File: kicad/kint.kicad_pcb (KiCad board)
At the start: 2 copper layers, 107.9 x 86 mm, 24 parts, among them J1 THUMB_RIGHT_SPC_KB600, J2 LEFT_13_LT, J3 TOP_LEFT, J4 TOP_RIGHT, J5 THUMB_LEFT_BAK, J6 THUMB_RIGHT_SPC, J7 RIGHT_13_DOWN, J8 THUMB_LEFT_BAK_KB600, U1 TEENSY_3.5/3.6

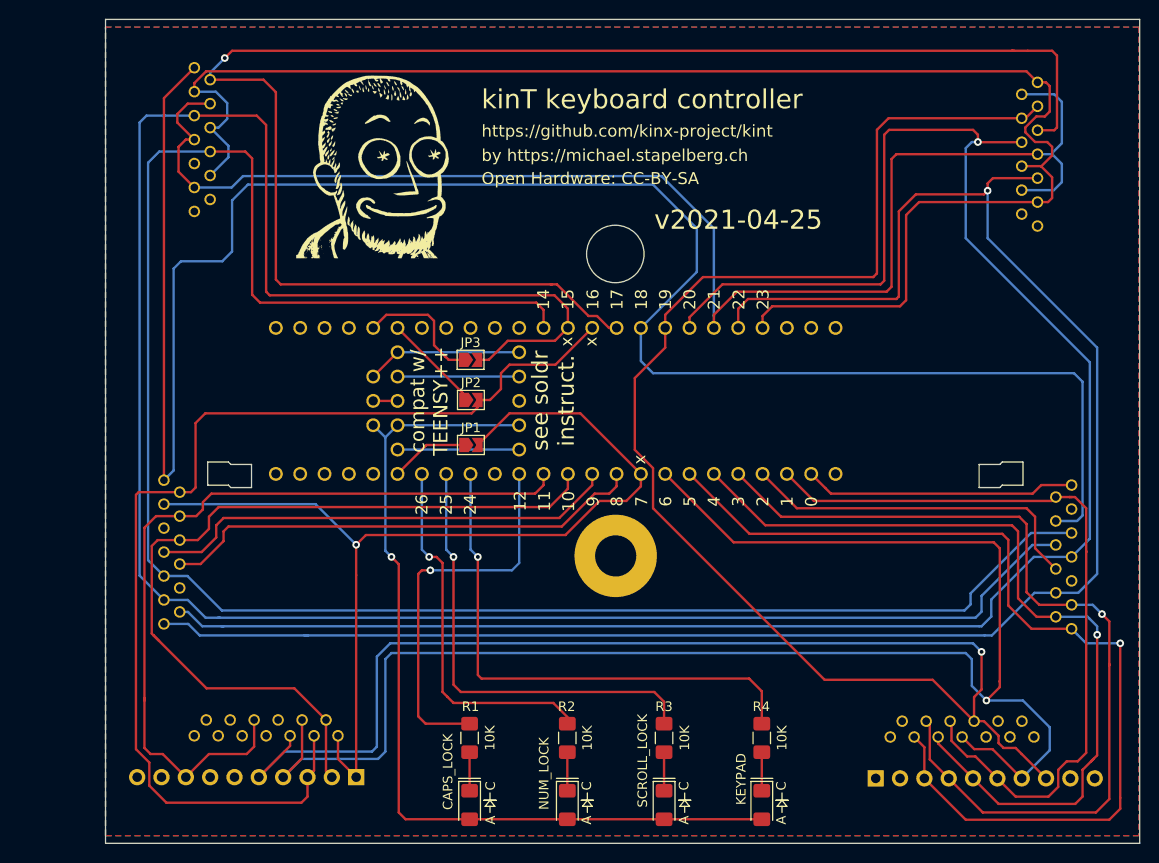
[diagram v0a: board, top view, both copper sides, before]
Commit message: Add more jumpers for Teensy++ 2.0 compat
This avoids requiring folks to pull pins out of headers for Teensy++ 2.0
compatibility, instead just requiring them to cut the traces, which I
think is better and more importantly is reversible, so that if someone
builds with a Teensy++ 2.0 and then wants to replace it with a 3.6, they
can just re-close the new jumpers, desolder the old ones, and be good to
go.
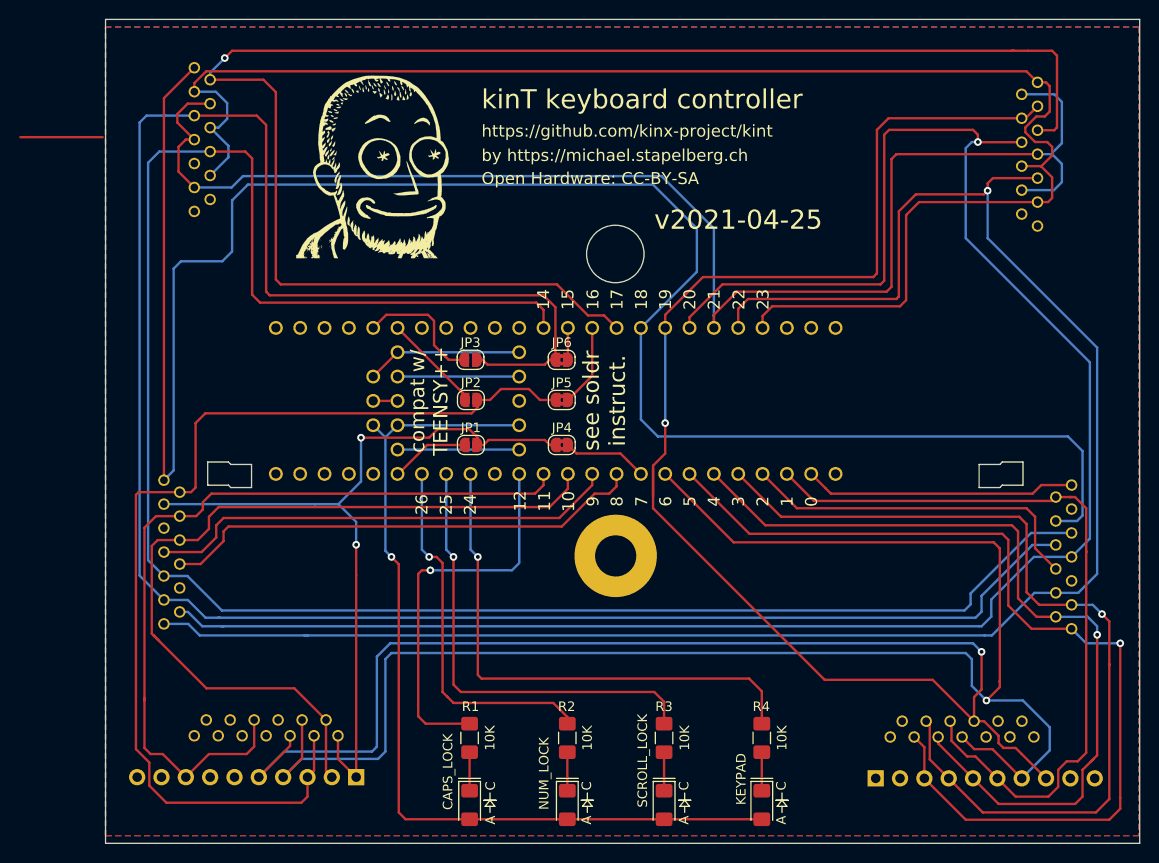
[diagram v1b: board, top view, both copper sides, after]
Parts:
- added JP4: SolderJumper_2_Bridged, Jumper:SolderJumper-2_P1.3mm_Bridged2Bar_RoundedPad1.0x1.5mm, F.Cu at (142.9, 106.4)
- added JP5: SolderJumper_2_Bridged, Jumper:SolderJumper-2_P1.3mm_Bridged2Bar_RoundedPad1.0x1.5mm, F.Cu at (142.9, 101.7)
- added JP6: SolderJumper_2_Bridged, Jumper:SolderJumper-2_P1.3mm_Bridged2Bar_RoundedPad1.0x1.5mm, F.Cu at (142.9, 97.5)
- JP1, JP2, JP3: footprint Jumper:SolderJumper-2_P1.3mm_Open_TrianglePad1.0x1.5mm -> Jumper:SolderJumper-2_P1.3mm_Open_RoundedPad1.0x1.5mm
- U1: value TEENSY_3.5/3.6 -> TEENSY_3.5_3.6
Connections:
- U1 pad 15/A1: /COL_2 -> Net-(JP6-Pad1)
- U1 pad 16/A2: /ROW_5 -> Net-(JP5-Pad1)
- U1 pad 7: /ROW_4 -> Net-(JP4-Pad2)
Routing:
- net /ROW_4: track 105.9 -> 83.1 mm, vias 1 -> 2
- net Net-(JP4-Pad2): track 0.00 -> 8.85 mm
- net (no net): track 0.00 -> 8.59 mm
- net Net-(JP5-Pad1): track 0.00 -> 8.57 mm
- net /ROW_5: track 115.6 -> 108.6 mm
- net Net-(JP6-Pad1): track 0.00 -> 3.33 mm
- net /COL_5: track 232.5 -> 233.9 mm, vias 1 -> 2
- net /COL_0: track 210.4 -> 209.7 mm
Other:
- board text removed: "x"
